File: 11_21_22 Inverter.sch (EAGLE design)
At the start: 32 parts, among them IC1 FAN73895MX, Q1 ROHM_SCT3022ALGC11ROHM_SCT302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, Q2 ROHM_SCT3022ALGC11ROHM_SCT302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, Q3 ROHM_SCT3022ALGC11ROHM_SCT302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, Q4 ROHM_SCT3022ALGC11ROHM_SCT302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, Q5 ROHM_SCT3022ALGC11ROHM_SCT302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, Q6 ROHM_SCT3022ALGC11ROHM_SCT302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, U1 RASPBERRY_PICOTH

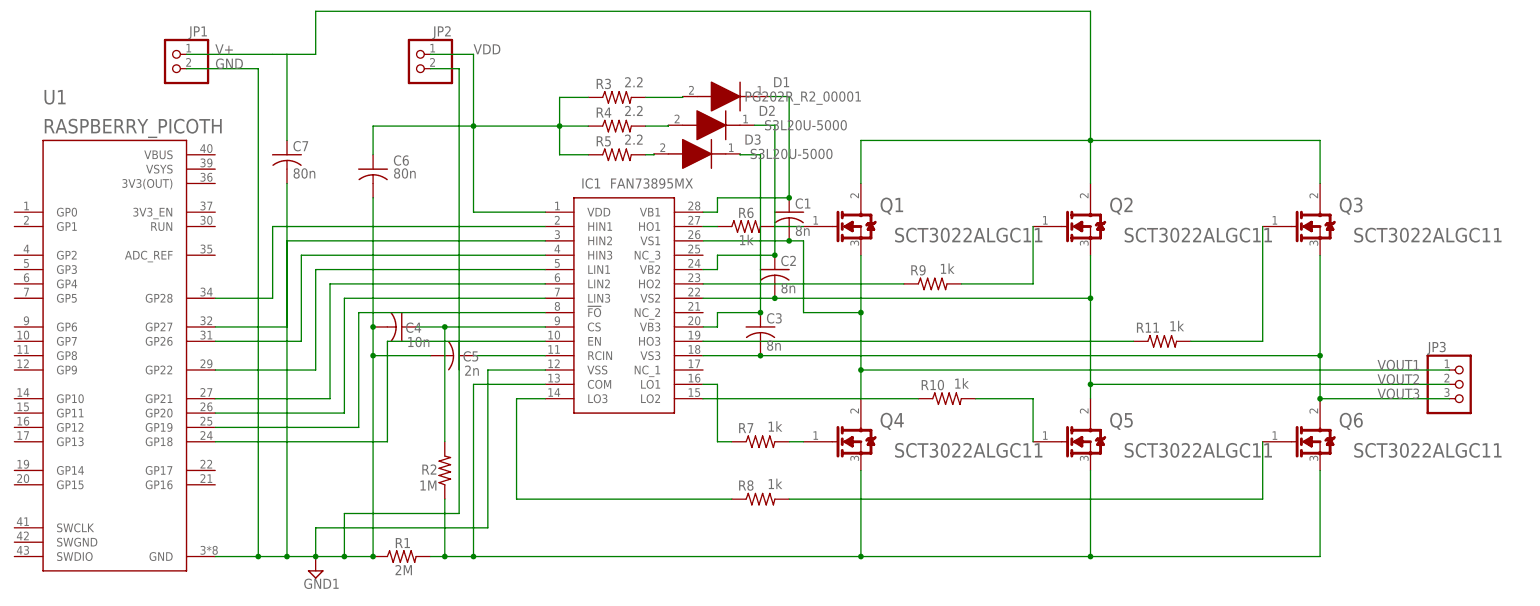
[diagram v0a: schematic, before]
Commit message: Updated inverter board and schematic with new IC
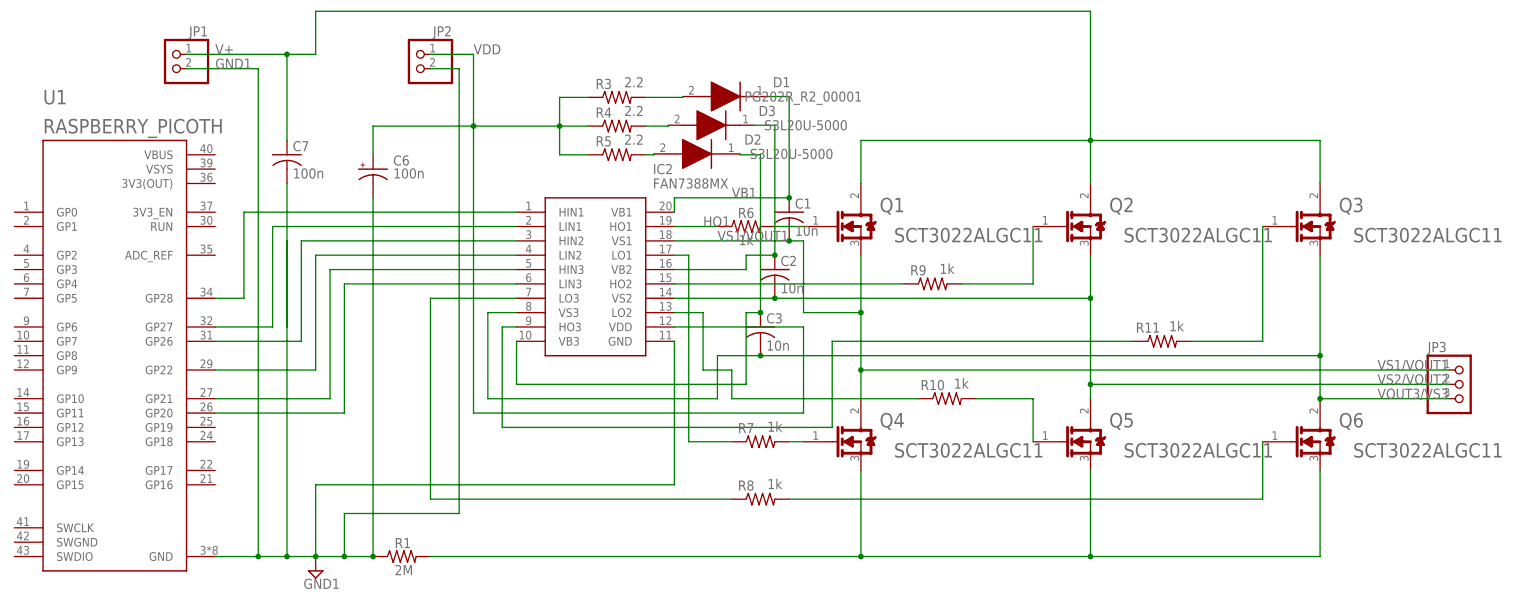
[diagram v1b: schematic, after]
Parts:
- removed C4: 10n, rcl:C-USC1206
- removed C5: 2n, rcl:C-USC1206
- removed IC1: FAN73895MX, FAN73895MX:FAN73895MX
- removed R2: 1M, rcl:R-US_0207/10
- added IC2: FAN7388MX, FAN7388MX:FAN7388MX
- C1, C2, C3: value 8n -> 10n
- C6: value 80n -> 100n; device rcl:C-USC1206 -> rcl:CPOL-USSMCZ
- C7: value 80n -> 100n; device rcl:C-USC1206 -> rcl:C-US025-024X044
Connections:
- removed net GND: C4.2, C5.2, C6.2, C7.2, IC1.VSS, JP1.2, JP2.2, R1.1, U1.GND
- removed net N$13: IC1.HO2, R9.1
- removed net N$15: IC1.LO2, R10.1
- removed net N$17: C1.1, D1.K, IC1.VB1
- removed net N$18: C2.1, D2.K, IC1.VB2
- removed net N$19: C3.1, D3.K, IC1.VB3
- removed net N$20: IC1.HIN2, U1.GP27
- removed net N$21: C5.1, IC1.RCIN
- removed net N$22: IC1.HIN3, U1.GP26
- removed net N$23: IC1.LIN1, U1.GP22
- removed net N$24: IC1.LIN2, U1.GP21
- removed net N$25: IC1.LIN3, U1.GP20
- removed net N$27: C4.1, IC1.CS, R2.2
- removed net VOUT1: C1.2, IC1.VS1, JP3.1, Q1.SOURCE, Q4.DRAIN
- removed net VOUT2: C2.2, IC1.VS2, JP3.2, Q2.SOURCE, Q5.DRAIN
- removed net VOUT3: C3.2, IC1.VS3, JP3.3, Q3.SOURCE, Q6.DRAIN
- new net COM/GND: Q4.SOURCE, Q5.SOURCE, Q6.SOURCE, R1.2
- new net GND1: C6.-, C7.2, IC2.GND, JP1.2, JP2.2, R1.1, U1.GND
- new net HO1: IC2.HO1, R6.1
- new net HO2: IC2.HO2, R9.1
- new net LO2: IC2.LO2, R10.1
- new net LO3: IC2.LO3, R8.1
- new net VB1: C1.1, D1.K, IC2.VB1
- new net VB2: C2.1, D3.K, IC2.VB2
- new net VB3: C3.1, D2.K, IC2.VB3
- new net VOUT3/VS3: C3.2, IC2.VS3, JP3.3, Q3.SOURCE, Q6.DRAIN
- new net VS1/VOUT1: C1.2, IC2.VS1, JP3.1, Q1.SOURCE, Q4.DRAIN
- new net VS2/VOUT2: C2.2, IC2.VS2, JP3.2, Q2.SOURCE, Q5.DRAIN
- net N$1: now also IC2.HIN1; no longer IC1.HIN1
- net N$12: now also IC2.HO3, R11.1; no longer IC1.EN, U1.GP18
- net N$2: now also IC2.LO1, R7.1; no longer IC1.COM, Q4.SOURCE, Q5.SOURCE, Q6.SOURCE, R1.2, R2.1
- net N$28: now also D3.A; no longer D2.A
- net N$29: now also D2.A; no longer D3.A
- net N$3: now also IC2.LIN1, U1.GP27; no longer IC1.HO3, R11.1
- net N$4: now also IC2.HIN2, U1.GP26; no longer IC1.HO1, R6.1
- net N$5: now also IC2.LIN2, U1.GP22; no longer IC1.!FO, U1.GP19
- net N$7: now also IC2.HIN3, U1.GP21; no longer IC1.LO1, R7.1
- net N$9: now also IC2.LIN3, U1.GP20; no longer IC1.LO3, R8.1
- net VDD: now also C6.+, IC2.VDD; no longer C6.1, IC1.VDD
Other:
- moved on the sheet: D2, D3
